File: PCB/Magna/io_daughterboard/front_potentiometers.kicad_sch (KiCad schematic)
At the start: 24 parts

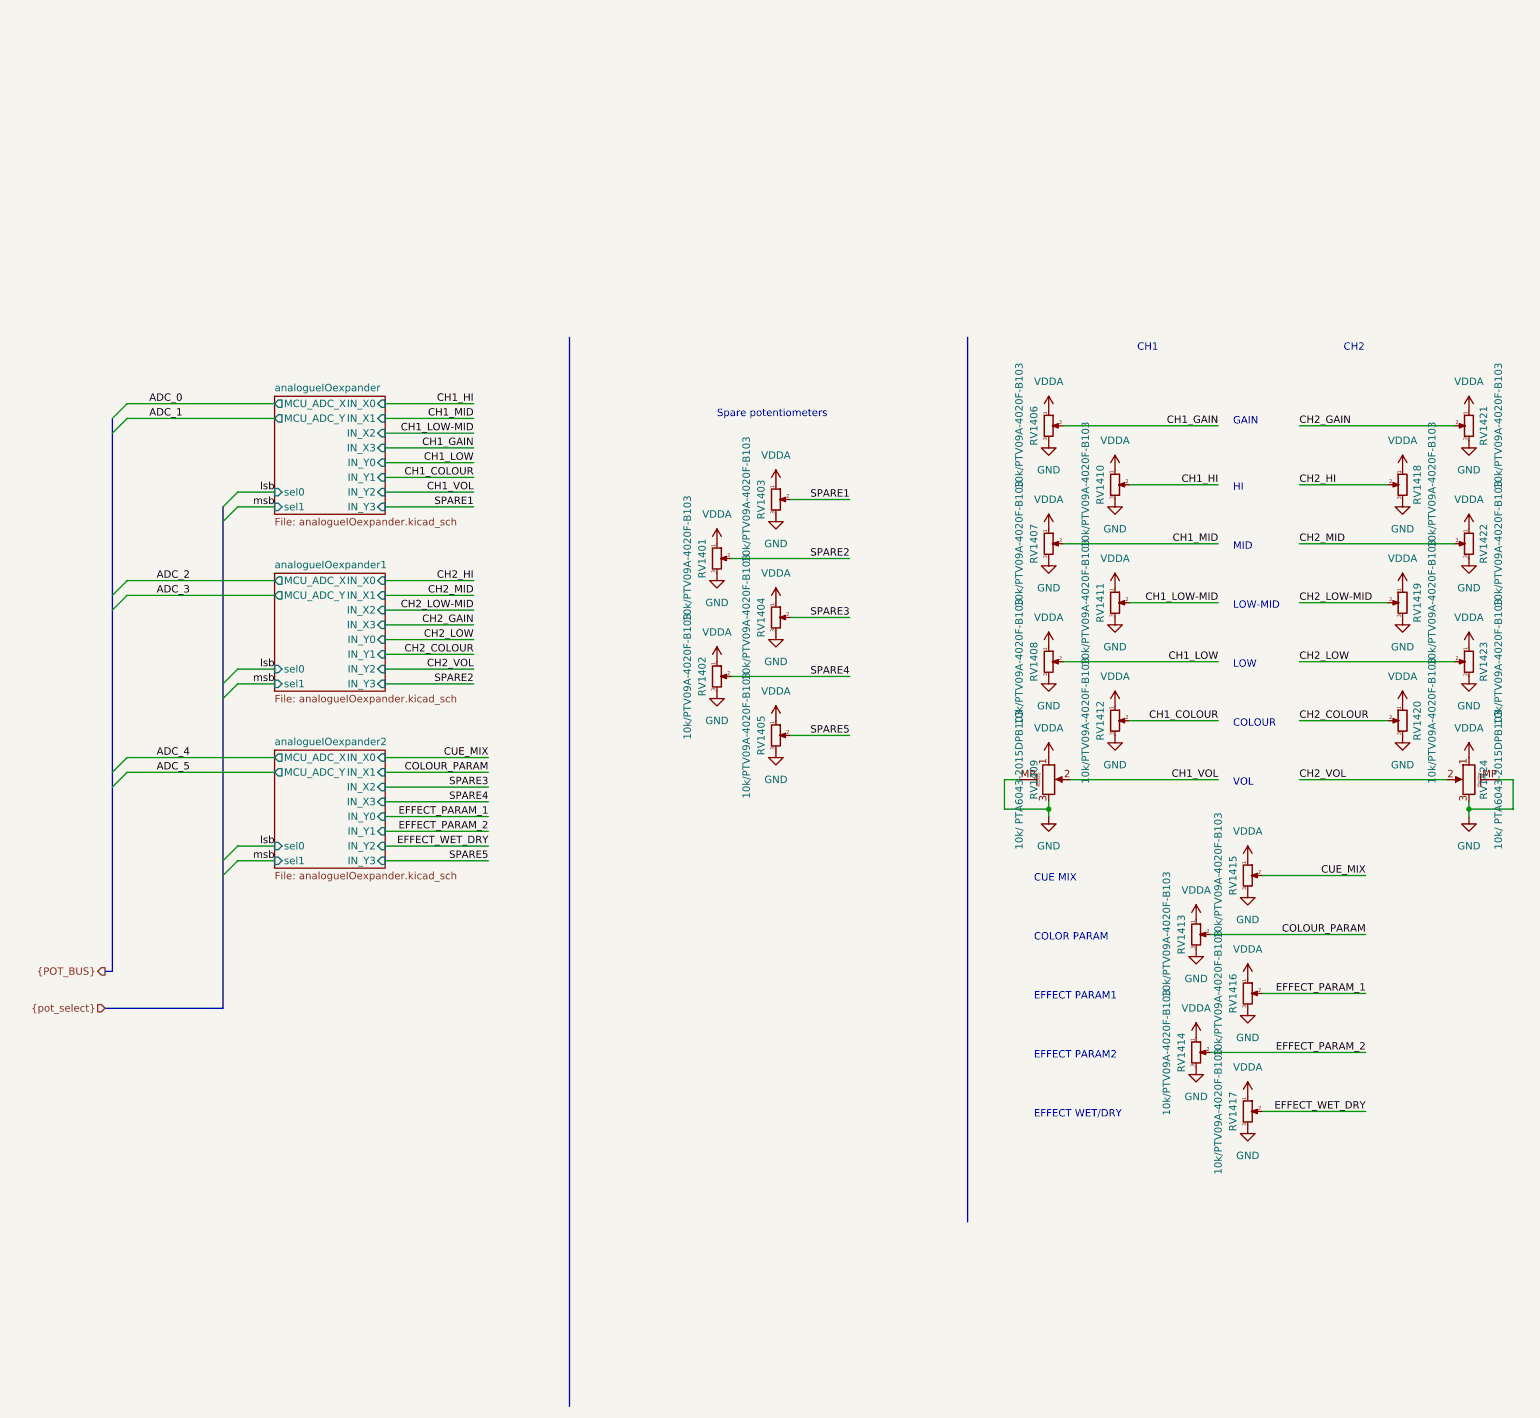
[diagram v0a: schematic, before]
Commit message: Split schematic to several projects
To allow for several boards to be done a kicad project
is needed for each
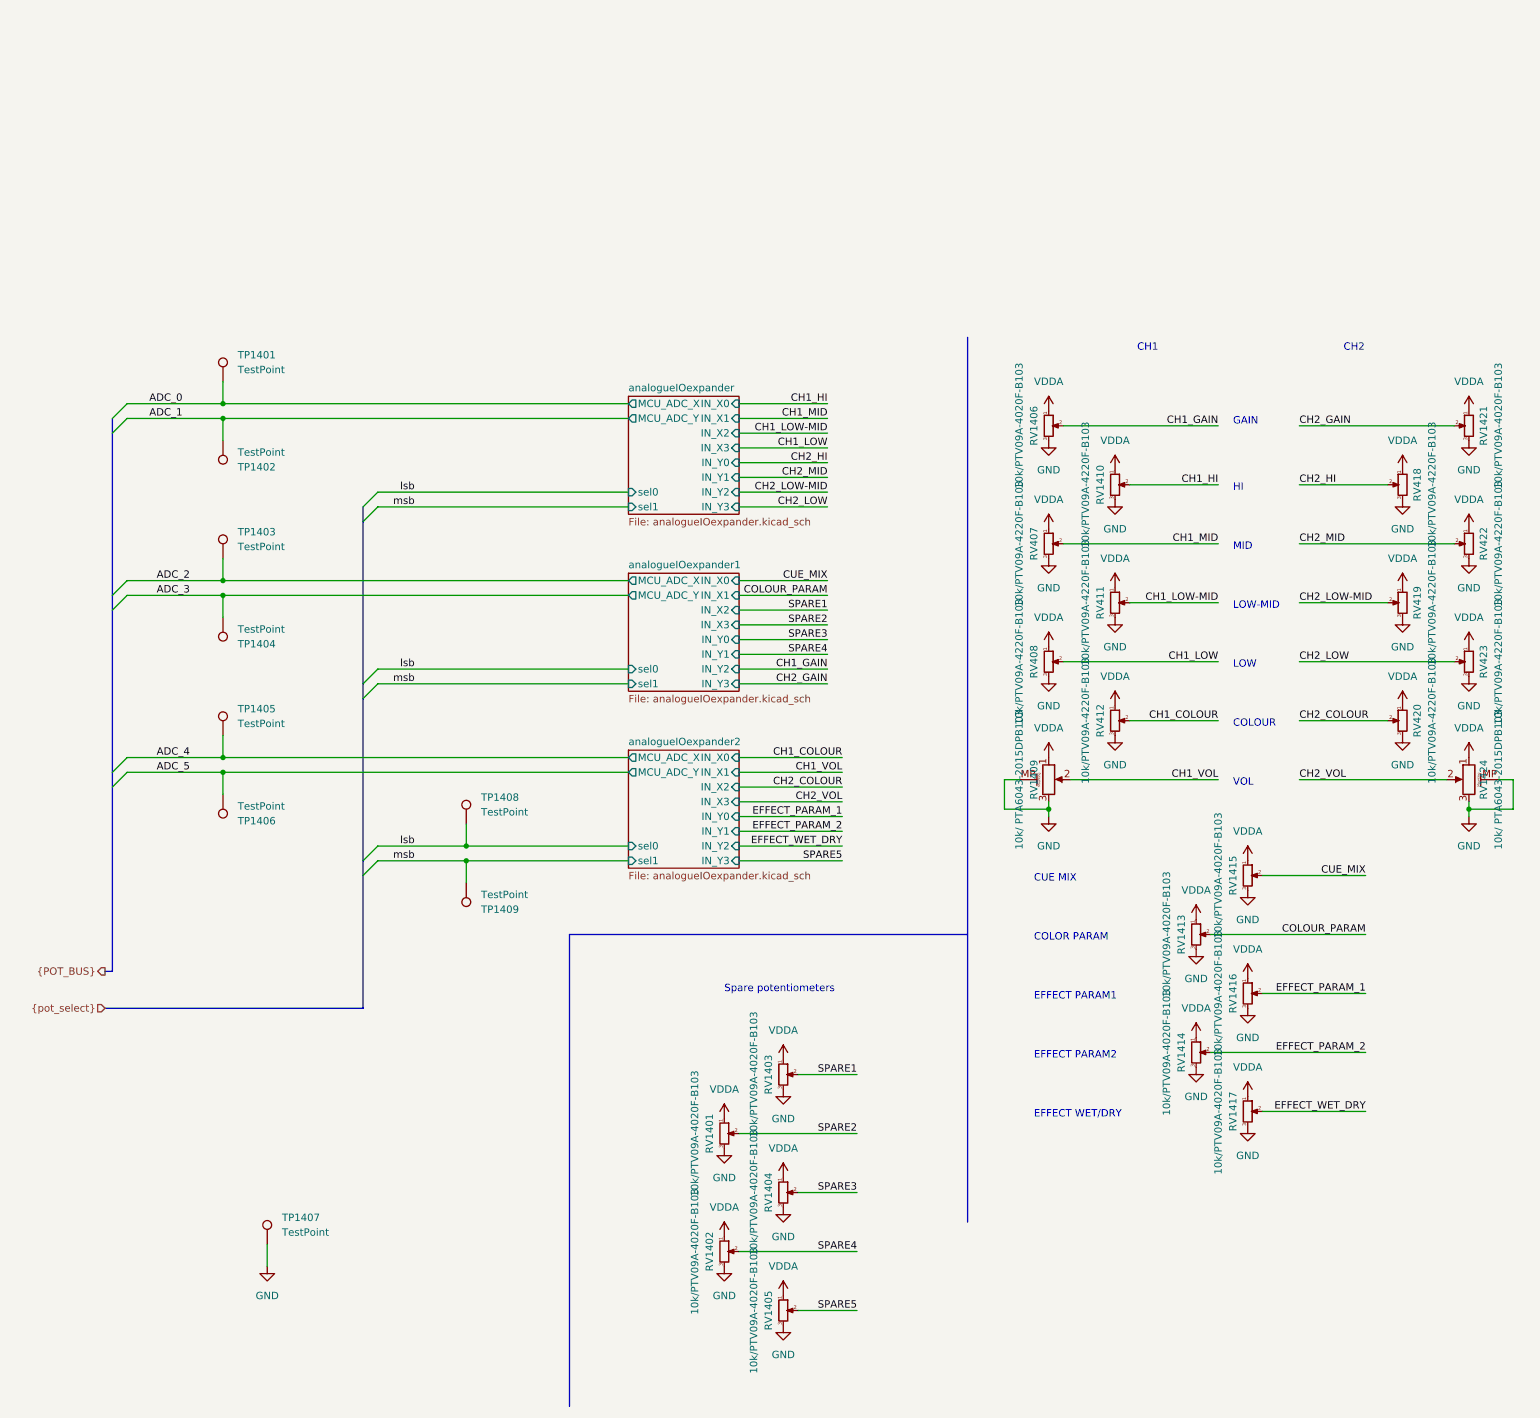
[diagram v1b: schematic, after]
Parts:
- removed RV1407, RV1408, RV1411, RV1412, RV1418, RV1419, RV1420, RV1422, RV1423: 10k/PTV09A-4020F-B103, Potentiometer_THT:Potentiometer_Bourns_PTV09A-1_Single_Vertical, symbol Device:R_Potentiometer_Small
- added RV407, RV408, RV411, RV412, RV418, RV419, RV420, RV422, RV423: 10k/PTV09A-4220F-B103, Potentiometer_THT:Potentiometer_Bourns_PTV09A-1_Single_Vertical, symbol Device:R_Potentiometer_Small
- added TP1401, TP1402, TP1403, TP1404, TP1405, TP1406, TP1407, TP1408, TP1409: TestPoint, TestPoint:TestPoint_Keystone_5005-5009_Compact, symbol Connector:TestPoint
- RV1410: value 10k/PTV09A-4020F-B103 -> 10k/PTV09A-4220F-B103
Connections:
- net ADC_0: now also TP1401.1
- net ADC_1: now also TP1402.1
- net ADC_2: now also TP1403.1
- net ADC_3: now also TP1404.1
- net ADC_4: now also TP1405.1
- net ADC_5: now also TP1406.1
- net CH1_COLOUR: now also RV412.2
- net CH1_LOW: now also RV408.2
- net CH1_LOW-MID: now also RV411.2
- net CH1_MID: now also RV407.2
- net CH2_COLOUR: now also RV420.2
- net CH2_HI: now also RV418.2
- net CH2_LOW: now also RV423.2
- net CH2_LOW-MID: now also RV419.2
- net CH2_MID: now also RV422.2
- net GND: now also RV407.3, RV408.3, RV411.3, RV412.3, RV418.3, RV419.3, RV420.3, RV422.3, RV423.3, TP1407.1
- net VDDA: now also RV407.1, RV408.1, RV411.1, RV412.1, RV418.1, RV419.1, RV420.1, RV422.1, RV423.1
- net lsb: now also TP1408.1
- net msb: now also TP1409.1
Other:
- moved on the sheet: RV1401, RV1402, RV1403, RV1404, RV1405

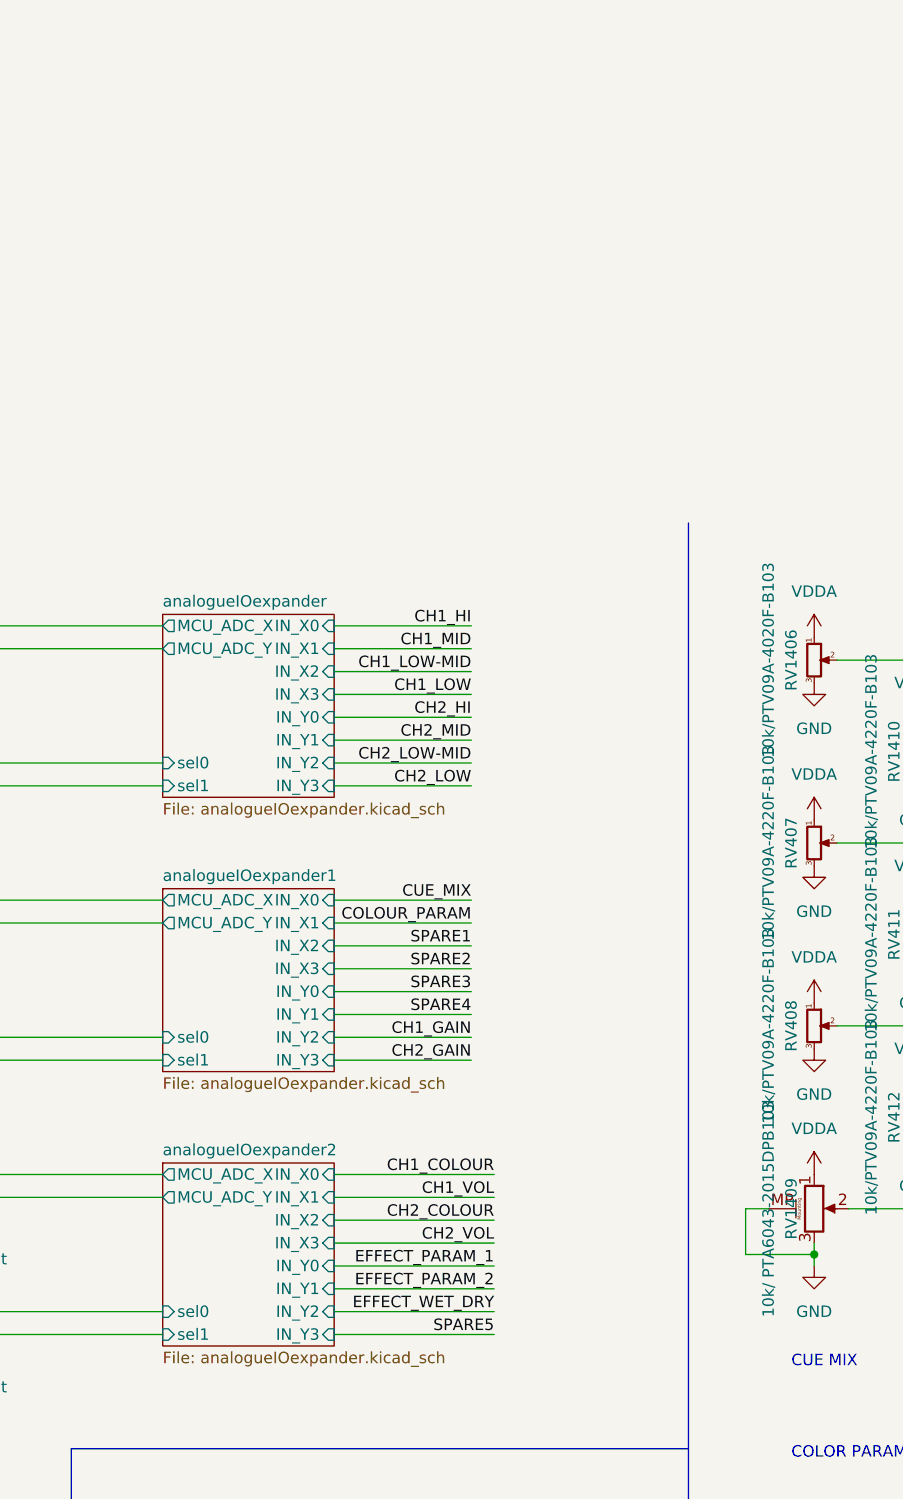
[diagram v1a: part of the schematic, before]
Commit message: Add a lot on the IO PCB
Also some schematic changes to accomodate issues found
when routing
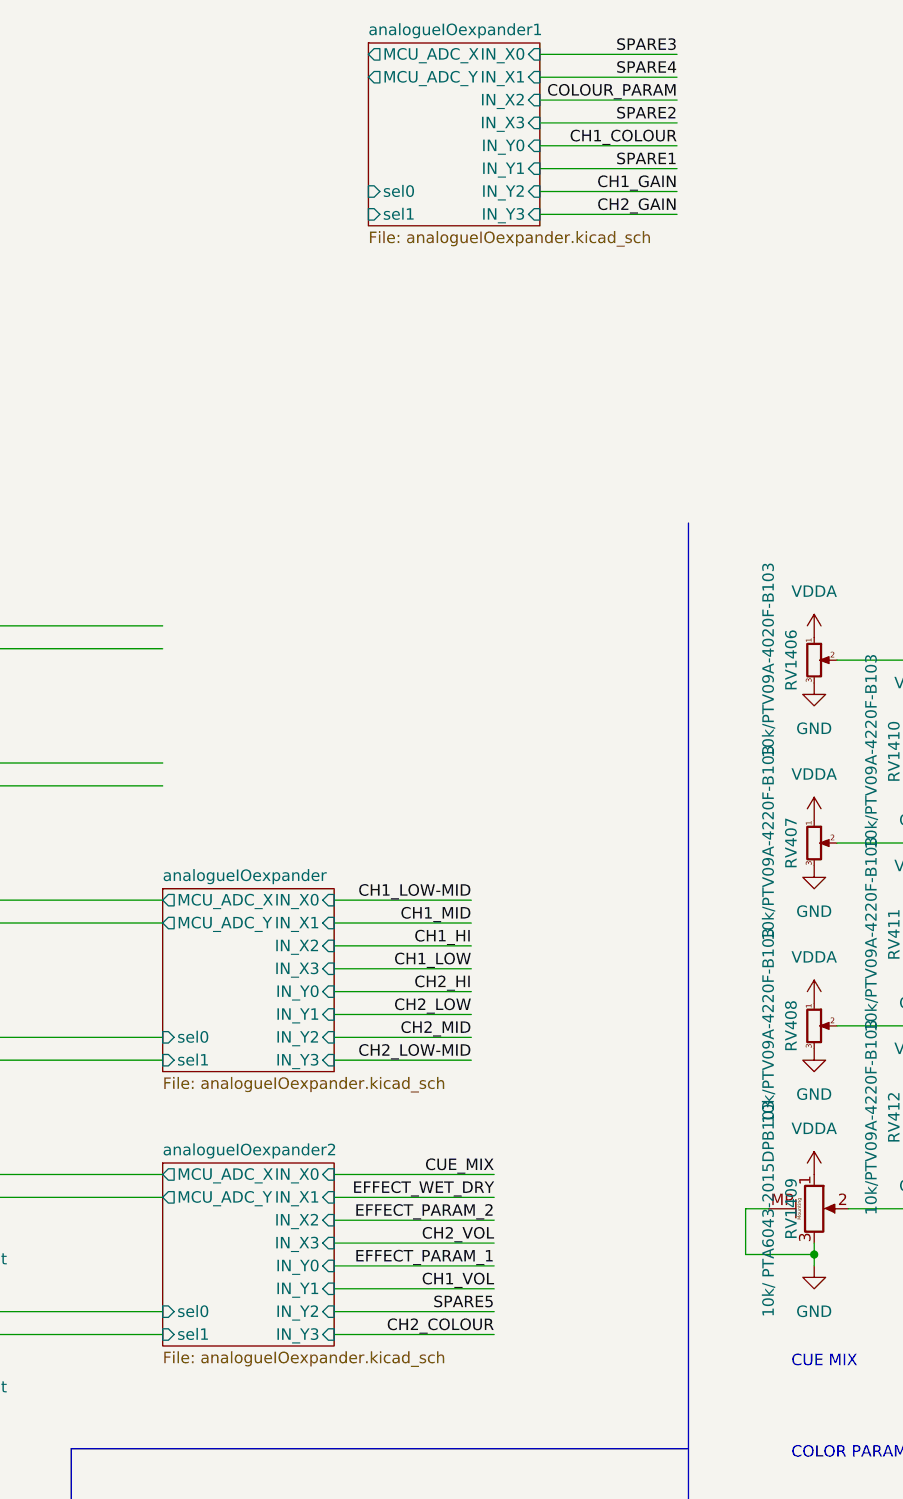
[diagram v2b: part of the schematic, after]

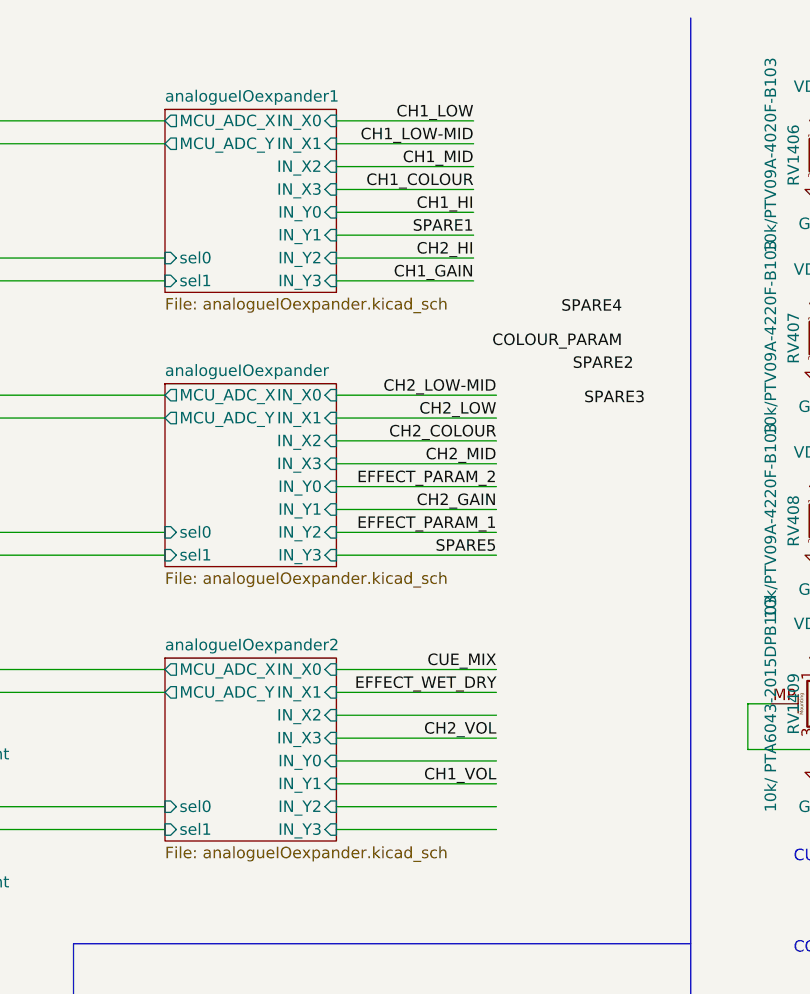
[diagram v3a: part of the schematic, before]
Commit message: Add more routing to IO Daugherboard
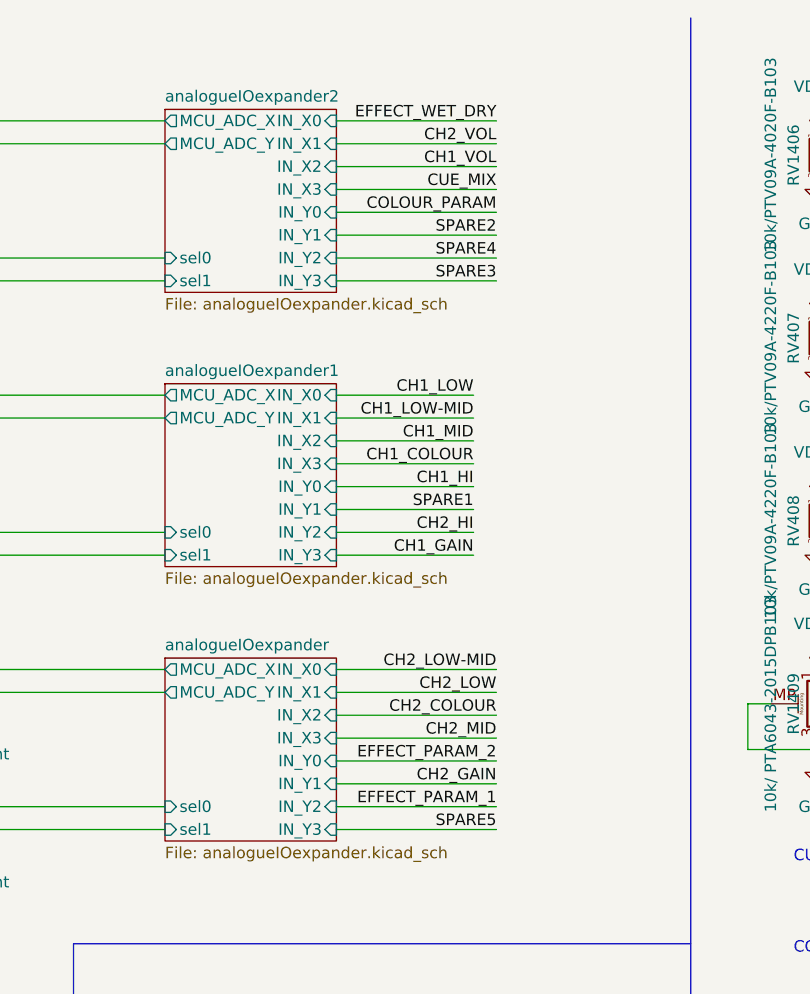
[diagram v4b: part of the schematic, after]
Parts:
- TP1401, TP1402, TP1403, TP1404, TP1405, TP1406, TP1407, TP1408, TP1409: footprint TestPoint:TestPoint_Keystone_5005-5009_Compact -> TestPoint:TestPoint_Keystone_5000-5004_Miniature
